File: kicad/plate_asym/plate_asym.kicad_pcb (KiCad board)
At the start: 2 copper layers, 231.6 x 92.5 mm, 65 parts, among them SW1 EC_SW, SW10 EC_SW, SW11 EC_SW, SW12 EC_SW, SW13 EC_SW, SW14 EC_SW, SW15 EC_SW, SW16 EC_SW, SW17 EC_SW, SW18 EC_SW, SW19 EC_SW, SW2 EC_SW, SW20 EC_SW, SW21 EC_SW, SW22 EC_SW, SW23 EC_SW, SW24 EC_SW, SW25 EC_SW, SW26 EC_SW, SW27 EC_SW, SW28 EC_SW, SW29 EC_SW, SW3 EC_SW, SW30 EC_SW, SW31 EC_SW, SW32 EC_SW, SW33 EC_SW, SW34 EC_SW, SW35 EC_SW, SW4 EC_SW, SW5 EC_SW, SW6 EC_SW, SW7 EC_SW, SW8 EC_SW, SW9 EC_SW

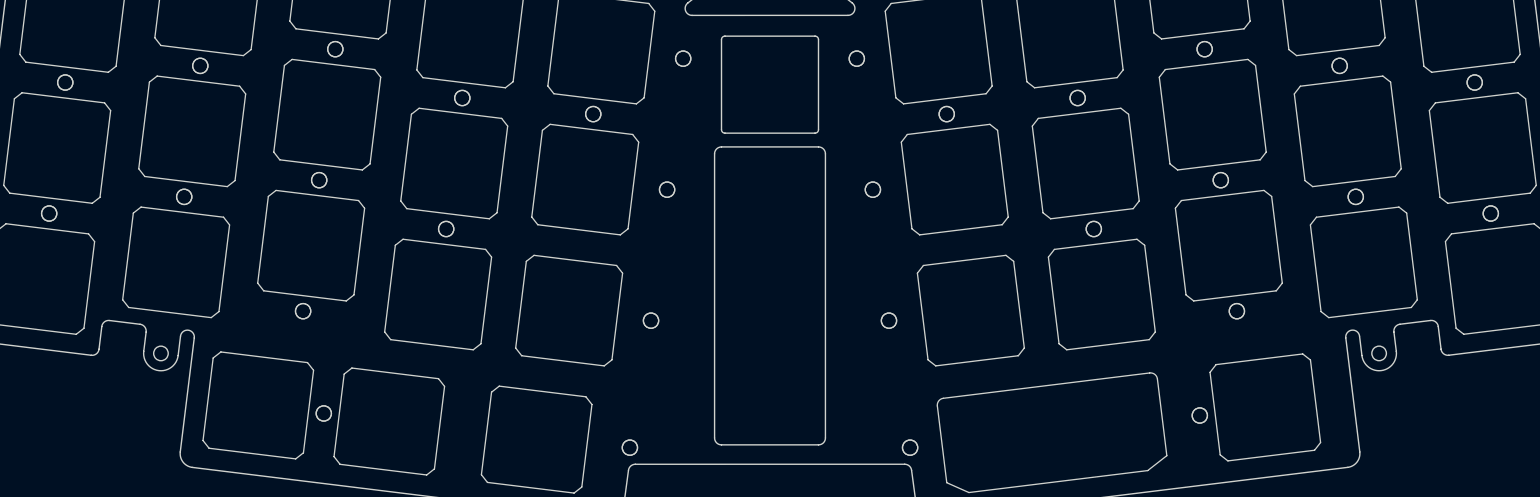
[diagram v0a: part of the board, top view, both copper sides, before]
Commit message: Making production plates
- Change EC mounting hole size from 2.2mm clearance to 1.6mm for M2
  tapping
- Reduce hole count for cost reduction
- Add drilling/fabrication notes
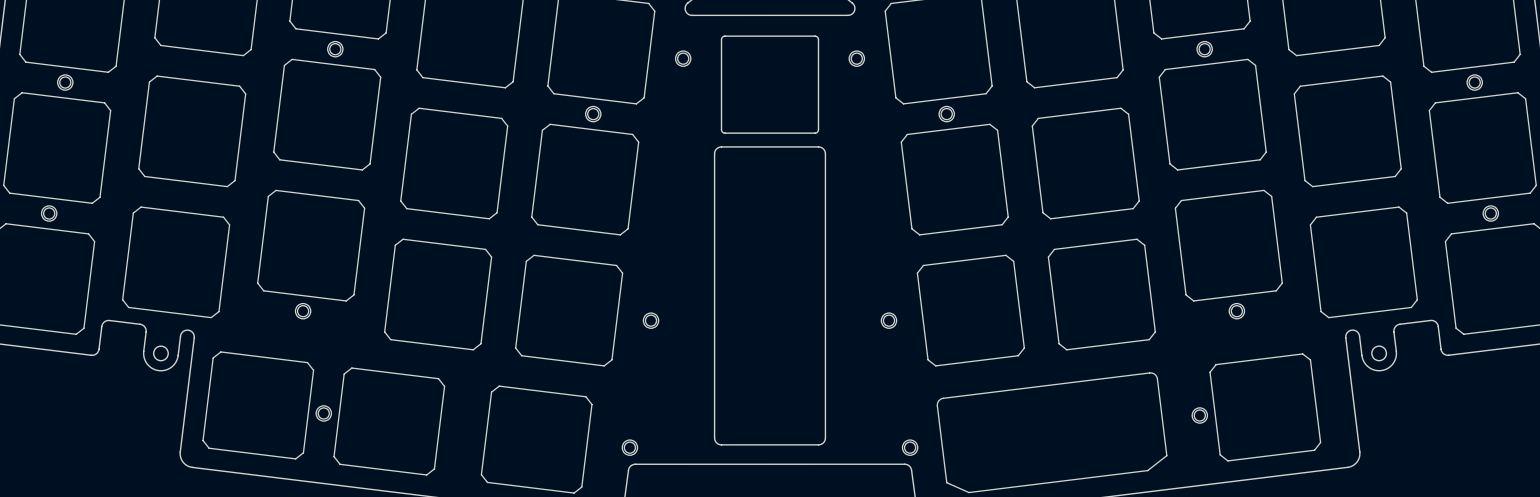
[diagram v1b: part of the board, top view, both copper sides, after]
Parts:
- removed H19, H20, H21, H22, H23, H24, H25, H26, H27, H28, H29, H30, H32, H33, H34: M2 Hole, capacitive_sensors:MountingHole_2.2mm_M2
- added H13: M2 Hole, capacitive_sensors:MountingHole_1.6mm_M2_tapped, F.Cu at (166.9, 136.8)
- added H5: M2 Hole, capacitive_sensors:MountingHole_1.6mm_M2_tapped, F.Cu at (134.1, 80.6)
- added H8: M2 Hole, capacitive_sensors:MountingHole_1.6mm_M2_tapped, F.Cu at (248.4, 84.1)
- H1, H10, H11, H12, H14, H15, H16, H17, H18, H2, H3, H4, H6, H7, H9: footprint capacitive_sensors:MountingHole_2.2mm_M2 -> capacitive_sensors:MountingHole_1.6mm_M2_tapped
- moved H16 152.8 mm to (208.7, 132.1)
- moved H18 149.4 mm to (250.7, 103.0)
- moved H6 80.2 mm to (209.4, 79.2)
- moved H11 41.8 mm to (121.1, 88.6)
- moved H17 37.2 mm to (82.2, 131.8), turned to 0 degrees
- moved H15 32.4 mm to (163.8, 118.4)
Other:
- board text added: "A"
- board text added: "B"
- board text added: "Plate Asym"
